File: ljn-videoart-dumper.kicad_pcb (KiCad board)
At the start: 2 copper layers, 68.6 x 53.3 mm, 13 parts, among them J1 Power, J2 Digital/PWM, J3 Analog, J4 Digital/PWM, J5 Video Art Edge, U1 74HC165, U2 74HC595, U3 74HC595

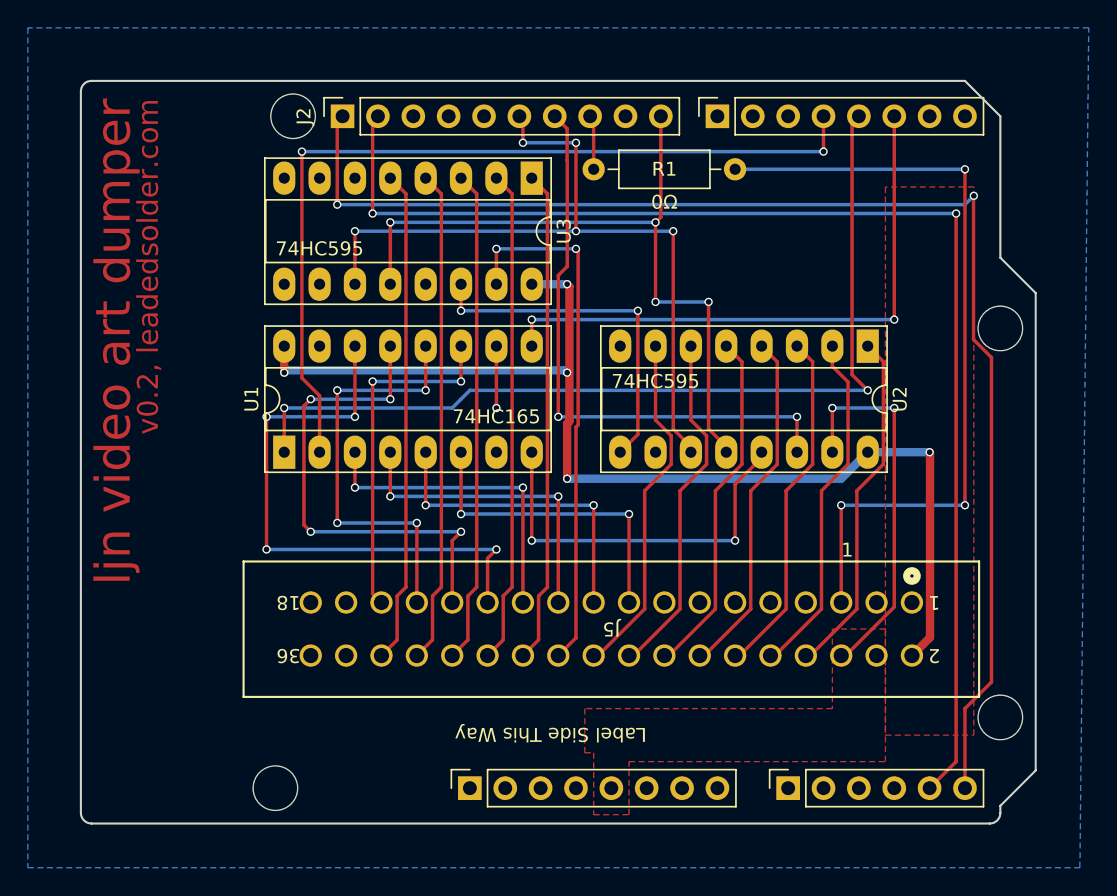
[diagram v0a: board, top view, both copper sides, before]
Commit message: Fix errors, add 5v/gnd test points
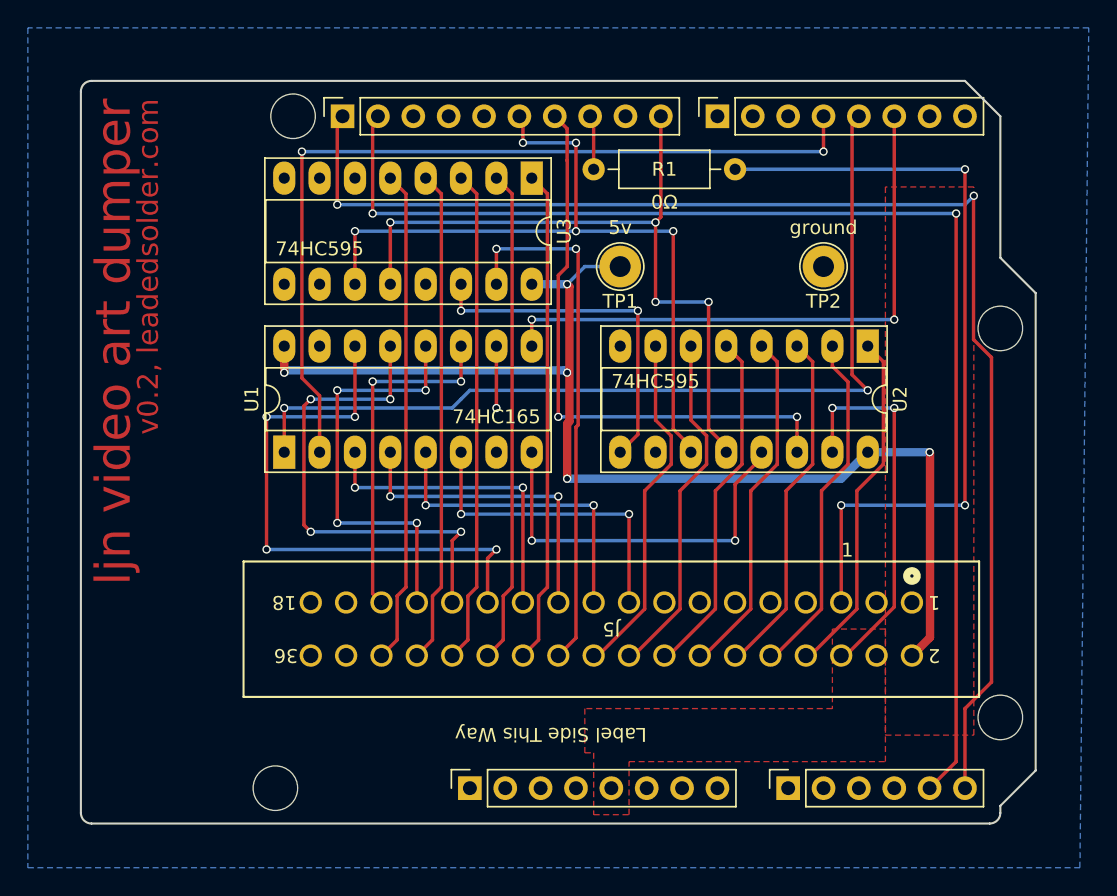
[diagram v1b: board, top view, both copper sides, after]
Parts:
- added TP1: 5v, TestPoint:TestPoint_Loop_D2.54mm_Drill1.5mm_Beaded, F.Cu at (138.7, 60.0)
- added TP2: ground, TestPoint:TestPoint_Loop_D2.54mm_Drill1.5mm_Beaded, F.Cu at (153.3, 60.0)
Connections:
- net /ROM_OE renamed /~{ROM_OE}
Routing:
- net +5V: track 81.0 -> 85.3 mm

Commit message: 5v/gnd markings
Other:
- board text added: "5V"
- board text added: "GND"
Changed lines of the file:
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@@
     )
+  )
+  (gr_text "5V" (at 138.862 93.904 90) (layer "B.SilkS")
+    (effects (font (size 1 1) (thickness 0.15)) (justify left bottom mirror))
   )
   (gr_text "d7" (at 140.005 82.855) (layer "B.SilkS")
@@
     (effects (font (size 1 1) (thickness 0.15)) (justify left bottom mirror))
   )
+  (gr_text "GND" (at 141.275 92.761 90) (layer "B.SilkS")
+    (effects (font (size 1 1) (thickness 0.15)) (justify left bottom mirror))
+  )
